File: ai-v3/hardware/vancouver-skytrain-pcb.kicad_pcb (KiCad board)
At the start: 2 copper layers, 200 x 109 mm, 85 parts, among them SW1 TS-1187A-B-A-B, SW2 TS-1187A-B-A-B, SW3 TS-1187A-B-A-B, SW4 TS-1187A-B-A-B, U1 XIAO-RP2040-DIP

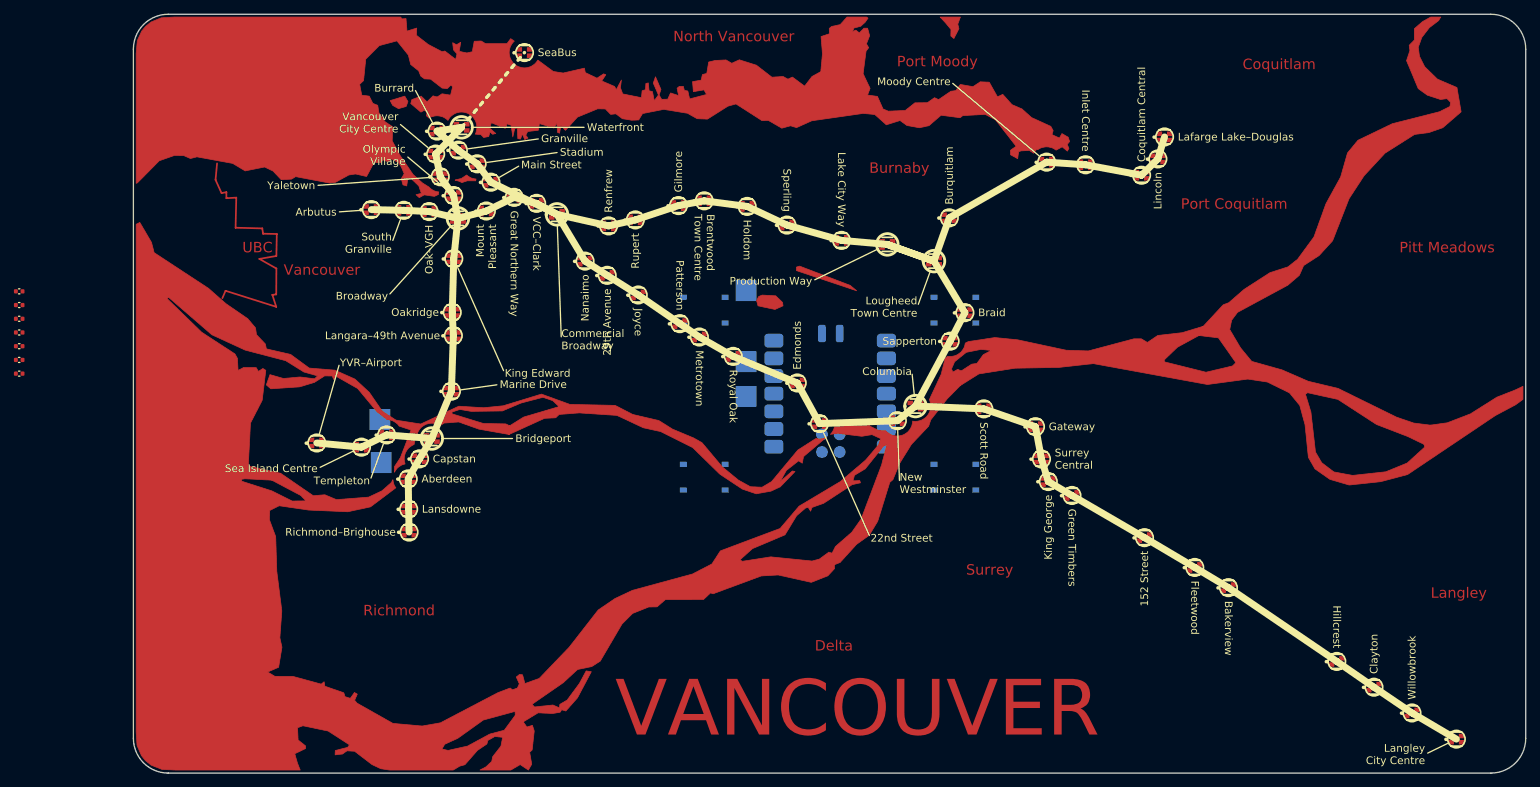
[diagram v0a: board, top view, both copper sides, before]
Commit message: Updated labels
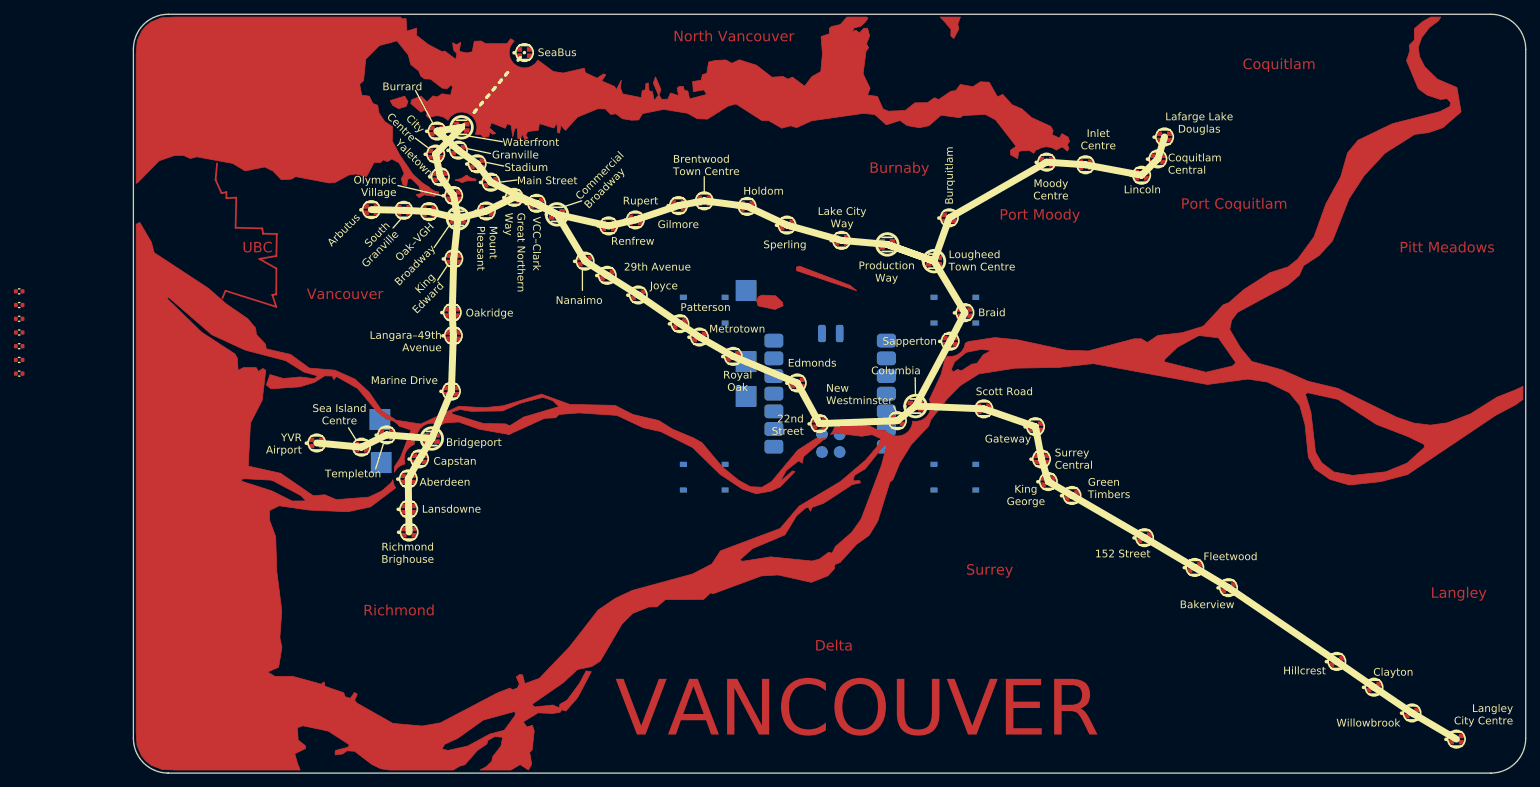
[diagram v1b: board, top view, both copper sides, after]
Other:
- board text added: "City Centre"
- board text added: "Lafarge Lake Douglas"
- board text added: "Richmond Brighouse"
- board text added: "YVR Airport"
- board text removed: "Lafarge Lake–Douglas"
- board text removed: "Richmond–Brighouse"
- board text removed: "Vancouver City Centre"
- board text removed: "YVR–Airport"
